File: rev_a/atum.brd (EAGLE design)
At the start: 18.8 x 19.6 mm, 41 parts, among them J1 EPIC2-HEADER2, J2 SH_MALE_2/1MM, U1 TPS62740, U2 FM25LBTDFN-8, U3 CC2538, U5 RV-3049-C3, X1 EPSON-FA-128, X3 ABS05-32.768KHZ-T

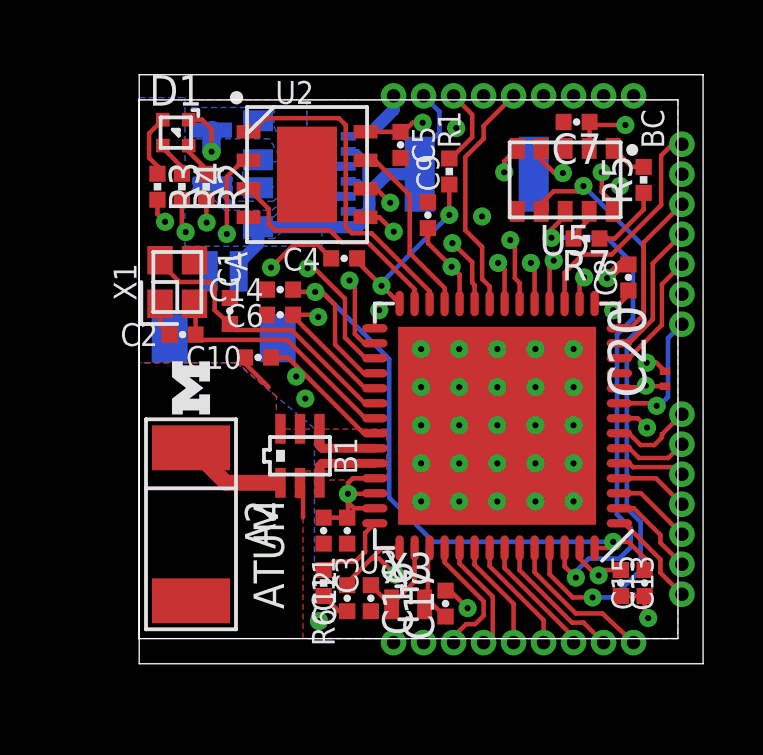
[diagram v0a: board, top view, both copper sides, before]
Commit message: updated silkscreen and names
- renumbered parts
- made silkscreen names for assembly
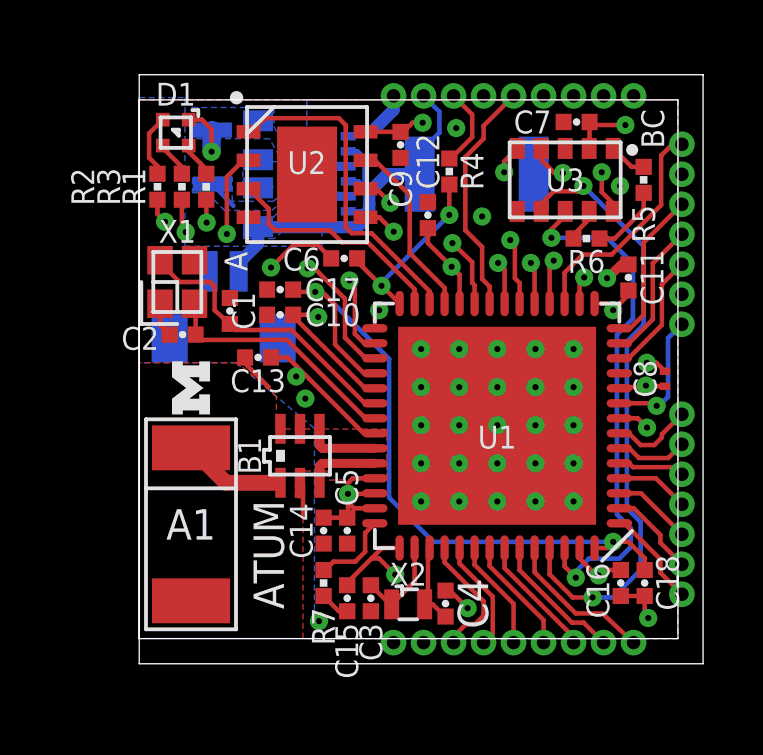
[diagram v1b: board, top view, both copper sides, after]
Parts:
- removed U5: RV-3049-C3, chips:MICRO-CRYSTAL-C3
- added U4: TPS62740, chips:R-PWSON-12
- C13, C14, C15: value 1uF -> 0.1uF
- C16, C17: value 22pF -> 1uF
- C18: value 10uF -> 1uF; device passives:0603_CAP -> passives:0402_CAP
- C20: value 0.1uF -> 10uF; device rcl:C0201 -> passives:0603_CAP
- C3: value 220pF -> 22pF
- C4: value 1nF -> 22pF
- C5: value 0.1uF -> 220pF
- C6: value 0.1uF -> 1nF
- C8: device passives:0402_CAP -> rcl:C0201
- R1: value 2.2k -> 1k
- R4: value 1k -> 2.2k
- R6: value 56k -> 10k
- R7: value 10k -> 56k
- U1: value TPS62740 -> CC2538; device chips:R-PWSON-12 -> chips:S-PVQFN-N56
- U3: value CC2538 -> RV-3049-C3; device chips:S-PVQFN-N56 -> chips:MICRO-CRYSTAL-C3
- moved C18 18.0 mm to (16.8, 1.85), flipped to the top, turned to 270 degrees
- moved C20 15.7 mm to (3.96, 16.6), flipped to the bottom, turned to 270 degrees
- moved R6 14.4 mm to (14.9, 13.3), turned to 180 degrees
- moved R7 14.4 mm to (6.15, 1.85), turned to 270 degrees
- moved C13 14.2 mm to (3.96, 9.37), turned to 180 degrees
- moved C11 13.2 mm to (16.3, 12.0), turned to 90 degrees
- moved C12 13.0 mm to (9.62, 14.1), turned to 90 degrees
- moved C5 13.0 mm to (6.93, 3.60)
- moved C4 12.0 mm to (10.2, 1.17), turned to 90 degrees
- moved C17 11.8 mm to (4.70, 11.6), turned to 180 degrees
- moved U1 10.3 mm to (11.9, 7.09), flipped to the top, turned to 180 degrees
- moved C15 9.93 mm to (6.93, 1.35)
- moved R4 8.93 mm to (10.3, 15.6)
- moved U3 8.50 mm to (14.2, 15.3)
- moved C16 8.35 mm to (16.1, 1.85)
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- renumbered A2 to A1, X3 to X2
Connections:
- net !FRAM_CS: now also U1.26; no longer U3.26
- net !FRAM_HOLD: now also U1.25; no longer U3.25
- net !FRAM_WP: now also U1.27; no longer U3.27
- net !RESET: now also R4.1; no longer R1.1
- net !RTC_INT: now also U1.53, U3.7; no longer U3.53, U5.7
- net ADC3: now also U1.19; no longer U3.19
- net ADC4: now also U1.20; no longer U3.20
- net ADC5: now also U1.21; no longer U3.21
- net ADC6: now also U1.22; no longer U3.22
- net ADC7: now also U1.23; no longer U3.23
- net B3: now also U1.52; no longer U3.52
- net B4: now also U1.51; no longer U3.51
- net B5: now also U1.50; no longer U3.50
- net B6: now also U1.49; no longer U3.49
- net BATTERY: now also C19.1, U4.1, U4.10, U4.12, U4.8; no longer C18.1, U1.1, U1.10, U1.12, U1.8
- net BOOTLOADER_CTRL: now also U1.18; no longer U3.18
- net BOOTLOADER_RX: now also U1.16; no longer U3.16
- net BOOTLOADER_TX: now also U1.17; no longer U3.17
- net C0: now also U1.14; no longer U3.14
- net C1: now also U1.13; no longer U3.13
- net C2: now also U1.12; no longer U3.12
- net C3: now also U1.11; no longer U3.11
- net DGND_USB: now also U1.1; no longer U3.1
- net DVDD_USB: now also U1.4; no longer U3.4
- net GND: now also R6.1, R7.2, U1.VSS_QFN, U3.6, U4.11, U4.3, U4.4, U4.9, U4.NC; no longer R6.2, R7.1, U1.11, U1.3, U1.4, U1.9, U1.NC, U3.VSS_QFN, U5.6
- net I2C_SCL: now also U1.9; no longer U3.9
- net I2C_SDA: now also U1.8; no longer U3.8
- net LED_BLUE: now also R3.2, U1.30; no longer R4.2, U3.30
- net LED_GREEN: now also R2.2, U1.31; no longer R3.2, U3.31
- net LED_RED: now also R1.2, U1.29; no longer R2.2, U3.29
- net N$1: now also C6.1, R4.2, U1.28; no longer C4.1, R1.2, U3.28
- net N$10: now also U1.35; no longer U3.35
- net N$11: now also R2.1; no longer R3.1
- net N$12: now also R3.1; no longer R4.1
- net N$13: now also C4.1, U1.45; no longer C17.1, U3.45
- net N$14: now also R6.2, U3.9; no longer R7.2, U5.9
- net N$15: now also C17.1, C18.1, U1.32, U1.56; no longer C14.1, C15.1, U3.32, U3.56
- net N$16: now also U3.1; no longer U5.1
- net N$5: now also U4.2; no longer U1.2
- net N$6: now also C3.1, U1.44; no longer C16.1, U3.44
- net N$7: now also R1.1; no longer R2.1
- net N$8: now also R7.1, U1.42; no longer R6.1, U3.42
- net N$9: now also U1.34; no longer U3.34
- net RF_N: now also U1.38; no longer U3.38
- net RF_P: now also U1.37; no longer U3.37
- net RTC_CE: now also U1.54, U3.8; no longer U3.54, U5.8
- net SPI_MISO: now also U1.5; no longer U5.5
- net SPI_MOSI: now also U1.6, U3.10; no longer U3.6, U5.10
- net SPI_SCK: now also U1.7, U3.4; no longer U3.7, U5.4
- net TCK: now also U1.47; no longer U3.47
- net TDO: now also U1.48; no longer U3.48
- net TMS: now also U1.46; no longer U3.46
- net USB_N: now also U1.3; no longer U3.3
- net USB_P: now also U1.2; no longer U3.2
- net VCC: now also C14.1, C15.1, C16.1, U1.10, U1.15, U1.24, U1.33, U1.36, U1.39, U1.40, U1.41, U1.43, U1.55, U3.2, U4.5; no longer C19.1, C3.1, C6.1, U1.5, U3.10, U3.15, U3.24, U3.33, U3.36, U3.39, U3.40, U3.41, U3.43, U3.55, U5.2
